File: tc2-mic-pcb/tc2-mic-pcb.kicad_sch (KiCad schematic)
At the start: 15 parts, among them J401 Conn_02x03_Odd_Even, J7 Screw_Terminal_01x01, U401 AP7335-18SNG-7, U402 TXS0102DCT

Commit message: Updated to use field LCSC Part instead of LCSC for the JLCPCB part number
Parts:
- C401, C402: LCSC C1525 -> (none); LCSC Part (none) -> C1525
- C403: LCSC C170182 -> (none); LCSC Part (none) -> C170182
- C404, C405, C406: LCSC C52923 -> (none); LCSC Part (none) -> C52923
- J401: LCSC C5160759 -> (none); LCSC Part (none) -> C5160759
- J7: LCSC C2928186 -> (none); LCSC Part (none) -> C2928186
- MK401: LCSC C2879853 -> (none); LCSC Part (none) -> C2879853
- R401, R402, R403: LCSC C25092 -> (none); LCSC Part (none) -> C25092
- U401: LCSC C460378 -> (none)
- U402: LCSC C324082 -> (none); LCSC Part (none) -> C324082
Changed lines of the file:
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@@
 			)
 		)
-		(property "LCSC" "C170182"
+		(property "LCSC Part" "C170182"
 			(at 76.2 45.72 0)
 			(effects
@@
 			)
 		)
-		(property "LCSC" "C1525"
+		(property "LCSC Part" "C1525"
 			(at 154.94 31.75 0)
 			(effects
@@
 			)
 		)
-		(property "LCSC" "C52923"
+		(property "LCSC Part" "C52923"
 			(at 81.28 95.25 0)
 			(effects
@@
 			)
 		)
-		(property "LCSC" "C5160759"
+		(property "LCSC Part" "C5160759"
 			(at 60.96 91.44 0)
 			(effects
@@
 			)
 		)
-		(property "LCSC" "C25092"
+		(property "LCSC Part" "C25092"
 			(at 186.69 54.61 90)
 			(effects
@@
 			)
 		)
-		(property "LCSC" "C52923"
+		(property "LCSC Part" "C52923"
 			(at 55.88 48.26 0)
 			(effects
@@
 			)
 		)
-		(property "LCSC" "C52923"
+		(property "LCSC Part" "C52923"
 			(at 22.86 48.26 0)
 			(effects
@@
 			)
 		)
-		(property "LCSC" "C25092"
+		(property "LCSC Part" "C25092"
 			(at 120.65 53.34 90)
 			(effects
@@
 			)
 		)
-		(property "LCSC" "C2879853"
+		(property "LCSC Part" "C2879853"
 			(at 93.98 50.8 0)
 			(effects
@@
 			)
 		)
-		(property "LCSC" "C2928186"
+		(property "LCSC Part" "C2928186"
 			(at 107.95 97.79 0)
 			(effects
@@
 			)
 		)
-		(property "LCSC" "C460378"
-			(at 39.37 48.26 0)
-			(effects
-				(font
-					(size 1.27 1.27)
-				)
-				(hide yes)
-			)
-		)
 		(pin "1"
 		)
@@
 			)
 		)
-		(property "LCSC" "C324082"
+		(property "LCSC Part" "C324082"
 			(at 160.02 52.07 0)
 			(effects
@@
 			)
 		)
-		(property "LCSC" "C1525"
+		(property "LCSC Part" "C1525"
 			(at 170.18 35.56 0)
 			(effects
@@
 			)
 		)
-		(property "LCSC" "C2928186"
+		(property "LCSC Part" "C2928186"
 			(at 107.95 92.71 0)
 			(effects
@@
 			)
 		)
-		(property "LCSC" "C25092"
+		(property "LCSC Part" "C25092"
 			(at 134.62 49.53 90)
 			(effects

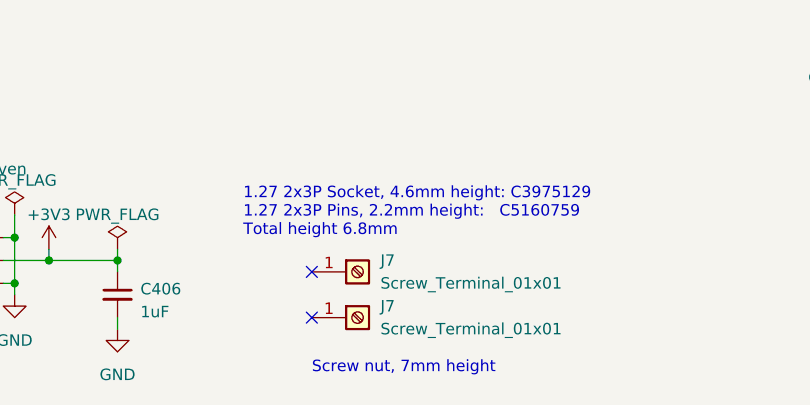
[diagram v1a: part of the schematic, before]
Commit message: Update to kicad 9, fix microphone panel v cuts
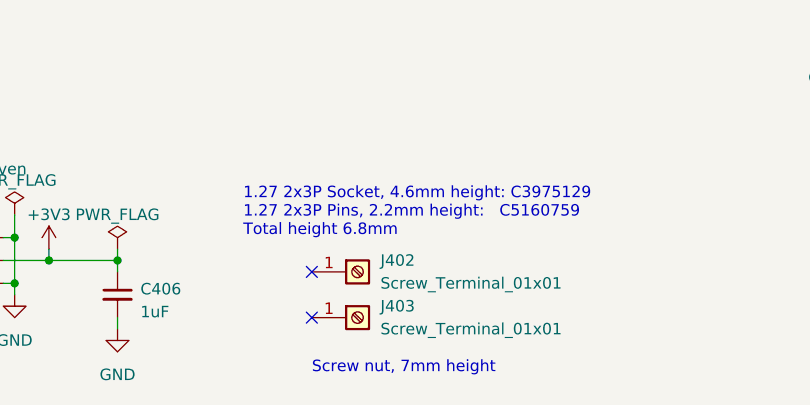
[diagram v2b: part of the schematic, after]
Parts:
- renumbered J7 to J402, J7 to J403
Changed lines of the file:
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@@
 (kicad_sch
-	(version 20231120)
+	(version 20250114)
 	(generator "eeschema")
-	(generator_version "8.0")
+	(generator_version "9.0")
 	(paper "A4")
+	(text "Use Class 1 Capacitor as \nspecified in the Mic Datasheet"
+		(exclude_from_sim no)
+		(at 66.04 35.56 0)
+		(effects
+			(font
+				(size 1.27 1.27)
+			)
+			(justify left bottom)
+		)
+	)
+	(text "Microphone"
+		(exclude_from_sim no)
+		(at 102.87 34.29 0)
+		(effects
+			(font
+				(size 2 2)
+			)
+			(justify left bottom)
+		)
+	)
+	(text "Screw nut, 7mm height"
+		(exclude_from_sim no)
+		(at 102.87 104.14 0)
+		(effects
+			(font
+				(size 1.27 1.27)
+			)
+			(justify left bottom)
+		)
+	)
+	(text "1.27 2x3P Socket, 4.6mm height: C3975129\n1.27 2x3P Pins, 2.2mm height:   C5160759\nTotal height 6.8mm"
+		(exclude_from_sim no)
+		(at 95.25 88.9 0)
+		(effects
+			(font
+				(size 1.27 1.27)
+			)
+			(justify left bottom)
+		)
+	)
 	(junction
 		(at 22.86 52.07)
@@
 		)
 	)
-	(text "Use Class 1 Capacitor as \nspecified in the Mic Datasheet"
-		(exclude_from_sim no)
-		(at 66.04 35.56 0)
-		(effects
-			(font
-				(size 1.27 1.27)
-			)
-			(justify left bottom)
-		)
-	)
-	(text "Microphone"
-		(exclude_from_sim no)
-		(at 102.87 34.29 0)
-		(effects
-			(font
-				(size 2 2)
-			)
-			(justify left bottom)
-		)
-	)
-	(text "Screw nut, 7mm height"
-		(exclude_from_sim no)
-		(at 102.87 104.14 0)
-		(effects
-			(font
-				(size 1.27 1.27)
-			)
-			(justify left bottom)
-		)
-	)
-	(text "1.27 2x3P Socket, 4.6mm height: C3975129\n1.27 2x3P Pins, 2.2mm height:   C5160759\nTotal height 6.8mm"
-		(exclude_from_sim no)
-		(at 95.25 88.9 0)
-		(effects
-			(font
-				(size 1.27 1.27)
-			)
-			(justify left bottom)
-		)
-	)
 	(label "CLOCK"
 		(at 106.68 50.8 0)
@@
 		(on_board yes)
 		(dnp no)
-		(property "Reference" "J7"
+		(property "Reference" "J403"
 			(at 110.49 96.52 0)
 			(effects
@@
 		(dnp no)
 		(fields_autoplaced yes)
-		(property "Reference" "#PWR085"
+		(property "Reference" "#PWR0410"
 			(at 76.2 55.88 0)
 			(effects
@@
 		(on_board yes)
 		(dnp no)
-		(property "Reference" "J7"
+		(property "Reference" "J402"
 			(at 110.49 91.44 0)
 			(effects
@@
 		)
 	)
+	(embedded_fonts no)
 )
